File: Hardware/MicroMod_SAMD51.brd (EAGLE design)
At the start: 22 x 22 mm, 36 parts, among them J2 MICROMOD-2222, U1 W25QXX128MBIT-6X5-NO_CENTER, U2 ATSAMD51J20A-A, Y1 32.768kHz

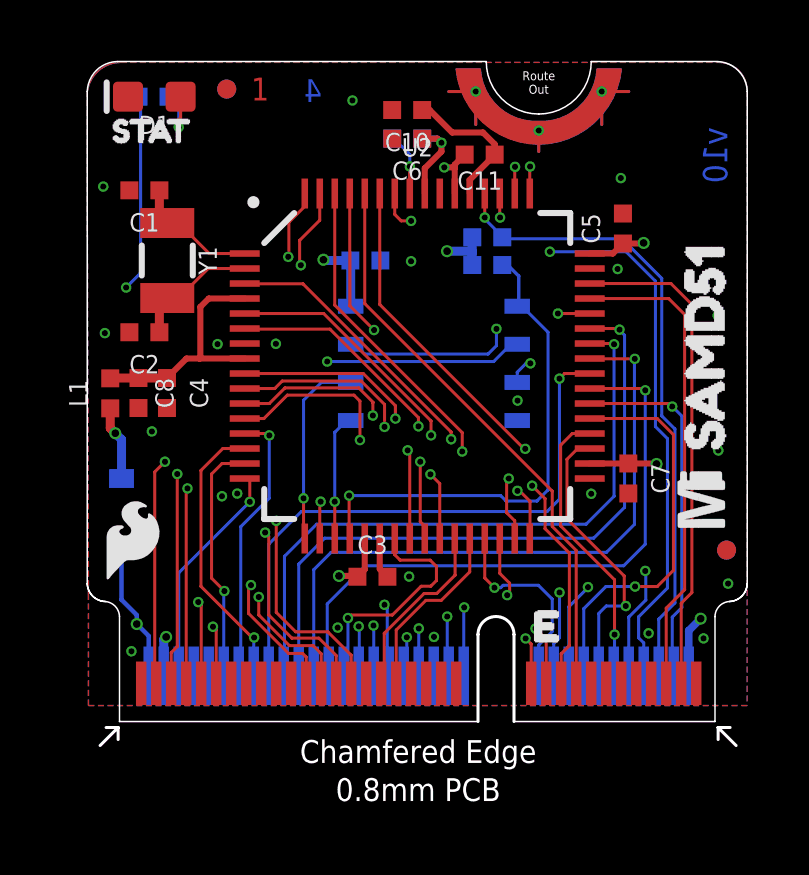
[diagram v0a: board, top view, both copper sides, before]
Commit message: Updates SparkFun silk, rolls version to v11, fixes some traces that were not crossing others at 90 degrees.
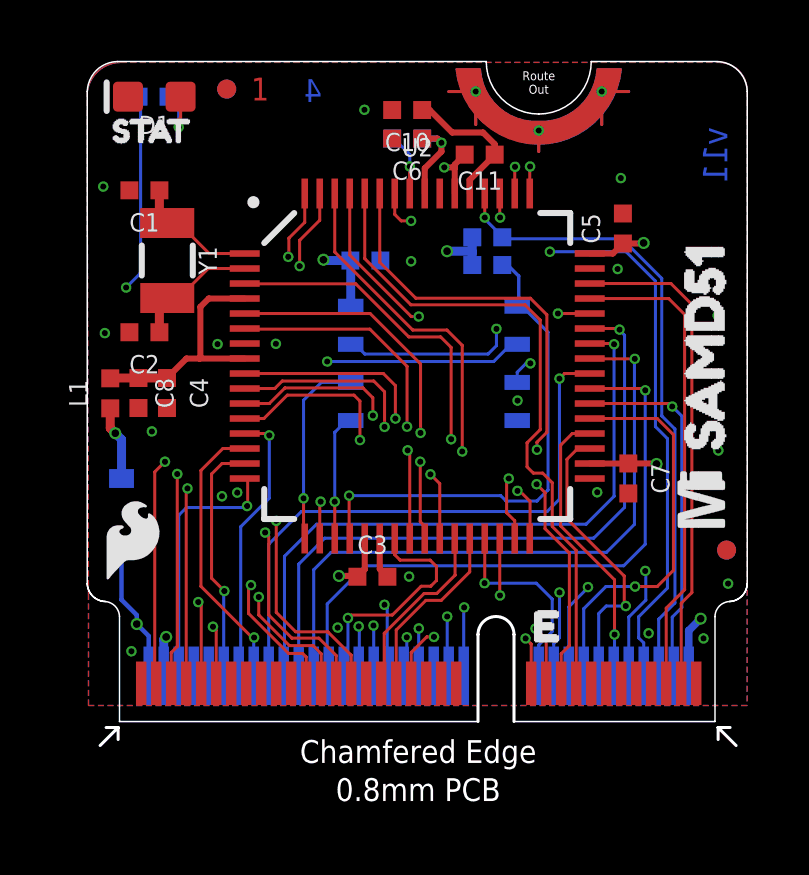
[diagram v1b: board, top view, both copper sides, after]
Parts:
- LOGO6: value SFE_LOGO_NAME_FLAME.1_INCH -> SFE_LOGO_NAME.1_INCH; device SparkFun-Aesthetics:SFE_LOGO_NAME_FLAME_.1 -> SparkFun-Aesthetics:SFE_LOGO_NAME_.1
- moved LOGO6 2.17 mm to (11.3, 7.40)
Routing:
- net TXO: track 19.2 -> 22.0 mm
- net RXI: track 19.1 -> 21.6 mm
- net GND: track 3.17 -> 5.17 mm
- net A0: track 17.1 -> 18.8 mm
- net !CS: track 7.72 -> 8.78 mm
- net D0: track 21.4 -> 22.3 mm
- net D1: track 20.2 -> 21.0 mm
- net A2/PWM0: track 17.9 -> 18.6 mm
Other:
- board text added: "v11"
- board text removed: "v10"

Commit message: Moves cap at top of board, adjusts USB differential pair
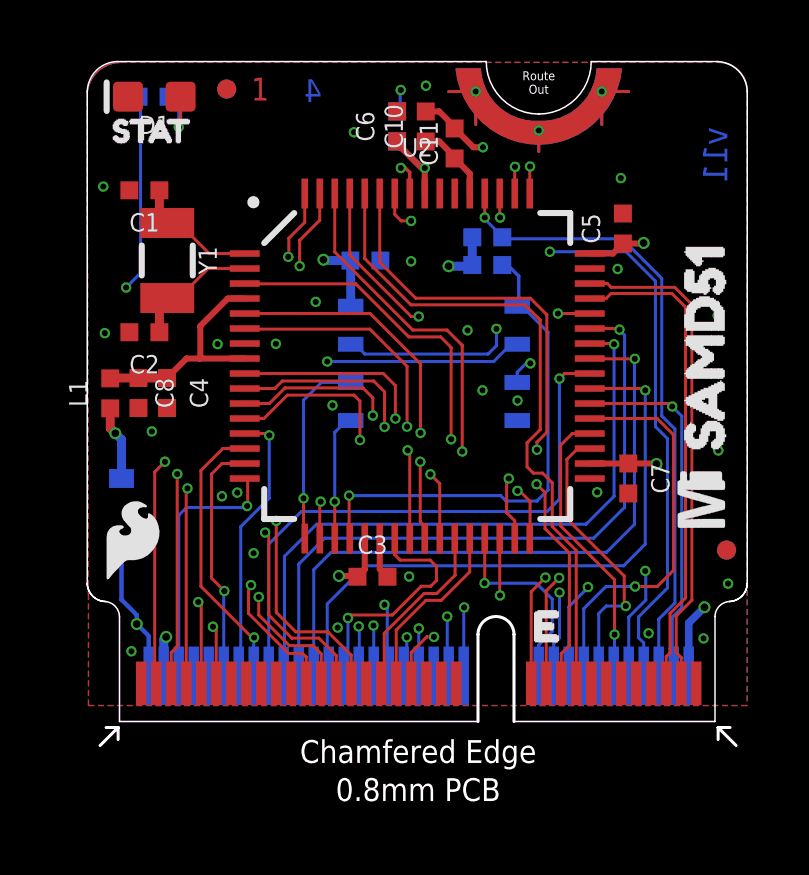
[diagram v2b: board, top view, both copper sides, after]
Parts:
- moved C11 0.91 mm to (12.2, 19.3), turned to 90 degrees
- moved C10 0.83 mm to (11.3, 19.8), turned to 90 degrees
- moved C6 0.53 mm to (10.3, 19.8), turned to 90 degrees
- moved R2 0.52 mm to (10.3, 19.8), turned to 270 degrees
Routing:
- net SWDCK: track 21.2 -> 24.8 mm, vias 2 -> 3
- net VCC: track 4.88 -> 2.61 mm
- net 3.3V_IN: track 27.9 -> 29.3 mm
- net SWDIO: track 18.4 -> 19.6 mm
- net GND: track 5.17 -> 5.76 mm, vias 21 -> 27

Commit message: Increases dimension line width, fixes some proportional text, relabels A0 to includ DAC
* Adds dimension measurements to measures layer
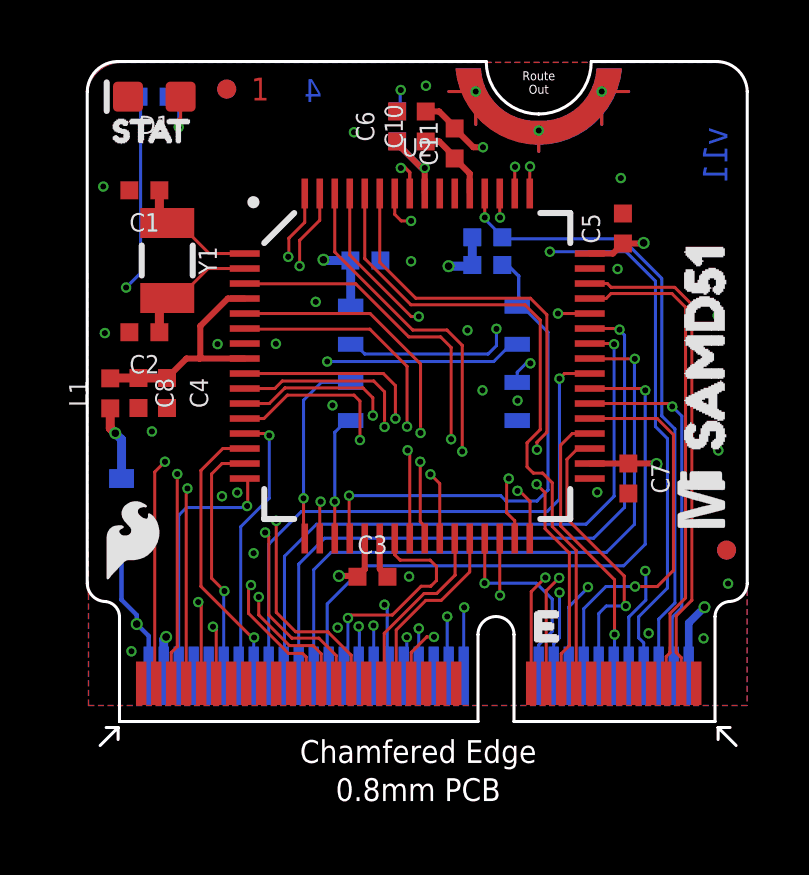
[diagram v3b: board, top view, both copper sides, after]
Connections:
- net A0 renamed A0/DAC
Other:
- board text removed: "Units in inches"
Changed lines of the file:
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@@
 <layers>
 <layer number="1" name="Top" color="4" fill="1" visible="yes" active="yes"/>
-<layer number="2" name="PWR_HORIZ" color="1" fill="3" visible="no" active="yes"/>
-<layer number="15" name="GND-VERT" color="4" fill="6" visible="no" active="yes"/>
+<layer number="2" name="PWR_HORIZ" color="1" fill="3" visible="yes" active="yes"/>
+<layer number="15" name="GND-VERT" color="4" fill="6" visible="yes" active="yes"/>
 <layer number="16" name="Bottom" color="3" fill="1" visible="yes" active="yes"/>
 <layer number="17" name="Pads" color="26" fill="1" visible="yes" active="yes"/>
@@
 <layer number="19" name="Unrouted" color="6" fill="1" visible="yes" active="yes"/>
 <layer number="20" name="Dimension" color="15" fill="1" visible="yes" active="yes"/>
-<layer number="21" name="tPlace" color="16" fill="1" visible="yes" active="yes"/>
-<layer number="22" name="bPlace" color="14" fill="1" visible="yes" active="yes"/>
+<layer number="21" name="tPlace" color="16" fill="1" visible="no" active="yes"/>
+<layer number="22" name="bPlace" color="14" fill="1" visible="no" active="yes"/>
 <layer number="23" name="tOrigins" color="15" fill="1" visible="yes" active="yes"/>
 <layer number="24" name="bOrigins" color="15" fill="1" visible="yes" active="yes"/>
@@
 <layer number="37" name="tTest" color="7" fill="1" visible="no" active="yes"/>
 <layer number="38" name="bTest" color="7" fill="1" visible="no" active="yes"/>
-<layer number="39" name="tKeepout" color="4" fill="11" visible="no" active="yes"/>
+<layer number="39" name="tKeepout" color="4" fill="11" visible="yes" active="yes"/>
 <layer number="40" name="bKeepout" color="1" fill="11" visible="no" active="yes"/>
 <layer number="41" name="tRestrict" color="4" fill="10" visible="no" active="yes"/>
@@
 <board>
 <plain>
-<text x="26.67" y="1.27" size="1.778" layer="47" font="vector" ratio="15">Units in inches</text>
-<dimension x1="0" y1="58.42" x2="0" y2="0" x3="-13.97" y3="29.21" textsize="1.27" textratio="15" layer="47" dtype="vertical" unit="inch"/>
-<dimension x1="2.54" y1="55.88" x2="0" y2="0" x3="-11.43" y3="27.94" textsize="1.27" textratio="15" layer="47" dtype="vertical" unit="inch"/>
-<dimension x1="0" y1="0" x2="2.286" y2="18.415" x3="-8.763" y3="9.2075" textsize="1.27" textratio="15" layer="47" dtype="vertical" unit="inch"/>
-<dimension x1="0" y1="0" x2="22.86" y2="0" x3="11.43" y3="-3.81" textsize="1.27" textratio="15" layer="47" dtype="horizontal" unit="inch"/>
-<dimension x1="0" y1="0" x2="2.54" y2="2.54" x3="1.27" y3="-6.35" textsize="1.27" textratio="15" layer="47" dtype="horizontal" unit="inch"/>
-<dimension x1="0" y1="0" x2="2.54" y2="2.54" x3="-6.35" y3="1.27" textsize="1.27" textratio="15" layer="47" dtype="vertical" unit="inch"/>
 <text x="31.62" y="32.94" size="1.778" layer="51" font="vector" ratio="15">0.8mm PCB
 45 degree chamfered edge
 Four layer design</text>
-<wire x1="0" y1="4.6" x2="0" y2="21" width="0.05" layer="20"/>
-<wire x1="22" y1="21" x2="22" y2="4.6" width="0.05" layer="20"/>
-<wire x1="21" y1="22" x2="22" y2="21" width="0.05" layer="20" curve="-87.205638"/>
-<wire x1="0" y1="21" x2="1" y2="22" width="0.05" layer="20" curve="-87.205638"/>
+<wire x1="0" y1="4.6" x2="0" y2="21" width="0.1016" layer="20"/>
+<wire x1="22" y1="21" x2="22" y2="4.6" width="0.1016" layer="20"/>
+<wire x1="21" y1="22" x2="22" y2="21" width="0.1016" layer="20" curve="-87.205638"/>
+<wire x1="0" y1="21" x2="1" y2="22" width="0.1016" layer="20" curve="-87.205638"/>
 <wire x1="0" y1="4.6" x2="0.6" y2="4" width="0.05" layer="20" curve="86.784874"/>
 <wire x1="21.4" y1="4" x2="22" y2="4.6" width="0.05" layer="20" curve="86.784874"/>
-<wire x1="20.925" y1="0" x2="14.225" y2="0" width="0.0508" layer="20"/>
-<wire x1="13.025" y1="0" x2="1.075" y2="0" width="0.0508" layer="20"/>
-<wire x1="1.075" y1="0" x2="1.075" y2="3.5" width="0.0508" layer="20"/>
-<wire x1="20.925" y1="3.5" x2="20.925" y2="0" width="0.0508" layer="20"/>
-<wire x1="21.4" y1="4" x2="20.925" y2="3.5" width="0.0508" layer="20" curve="84.949116"/>
-<wire x1="0.6" y1="4" x2="1.075" y2="3.5" width="0.0508" layer="20" curve="-83.820277"/>
+<wire x1="20.925" y1="0" x2="14.225" y2="0" width="0.1016" layer="20"/>
+<wire x1="13.025" y1="0" x2="1.075" y2="0" width="0.1016" layer="20"/>
+<wire x1="1.075" y1="0" x2="1.075" y2="3.5" width="0.1016" layer="20"/>
+<wire x1="20.925" y1="3.5" x2="20.925" y2="0" width="0.1016" layer="20"/>
+<wire x1="21.4" y1="4" x2="20.925" y2="3.5" width="0.1016" layer="20" curve="84.949116"/>
+<wire x1="0.6" y1="4" x2="1.075" y2="3.5" width="0.1016" layer="20" curve="-83.820277"/>
 <wire x1="14.225" y1="2.9" x2="14.225" y2="0" width="0.1016" layer="20"/>
 <wire x1="13.025" y1="2.9" x2="13.025" y2="0" width="0.1016" layer="20"/>
 <wire x1="14.225" y1="2.9" x2="13.025" y2="2.9" width="0.1016" layer="20" curve="180"/>
-<wire x1="21.4" y1="4" x2="22" y2="4.6" width="0.05" layer="20" curve="86.784874"/>
-<wire x1="0" y1="4.6" x2="0.6" y2="4" width="0.05" layer="20" curve="86.784874"/>
+<wire x1="21.4" y1="4" x2="22" y2="4.6" width="0.1016" layer="20" curve="86.784874"/>
+<wire x1="0" y1="4.6" x2="0.6" y2="4" width="0.1016" layer="20" curve="86.784874"/>
 <text x="21.336" y="19.812" size="0.8128" layer="16" font="vector" ratio="20" rot="SMR270">v11</text>
 <text x="23.114" y="-14.097" size="1.778" layer="51" font="vector">Elias Santistevan</text>
-<wire x1="1" y1="22" x2="13.3" y2="22" width="0.05" layer="20"/>
-<wire x1="16.8" y1="22" x2="21" y2="22" width="0.05" layer="20"/>
-<wire x1="13.3" y1="22" x2="15.05" y2="20.25" width="0.05" layer="20" curve="90"/>
-<wire x1="15.05" y1="20.25" x2="16.8" y2="22" width="0.05" layer="20" curve="90"/>
+<wire x1="1" y1="22" x2="13.3" y2="22" width="0.1016" layer="20"/>
+<wire x1="16.8" y1="22" x2="21" y2="22" width="0.1016" layer="20"/>
+<wire x1="13.3" y1="22" x2="15.05" y2="20.25" width="0.1016" layer="20" curve="90"/>
+<wire x1="15.05" y1="20.25" x2="16.8" y2="22" width="0.1016" layer="20" curve="90"/>
 <text x="5.461" y="20.701" size="0.762" layer="1" font="vector" ratio="15">1</text>
 <text x="6.041" y="20.681" size="0.762" layer="2" font="vector" ratio="15">2</text>
 <text x="6.651" y="20.661" size="0.762" layer="15" font="vector" ratio="15">3</text>
 <text x="7.822" y="20.651" size="0.762" layer="16" font="vector" ratio="15" rot="MR0">4</text>
+<dimension x1="13.025" y1="0" x2="1.075" y2="0" x3="7.05" y3="-5" textsize="1.27" textratio="15" layer="47" visible="yes"/>
+<dimension x1="20.925" y1="0" x2="14.225" y2="0" x3="17.575" y3="-5" textsize="1.27" textratio="15" layer="47" visible="yes"/>
+<dimension x1="20.925" y1="0" x2="21" y2="22" x3="27" y3="11" textsize="1.27" textratio="15" layer="47" dtype="vertical" visible="yes"/>
+<dimension x1="22" y1="21" x2="0" y2="21" x3="11" y3="26.5" textsize="1.27" textratio="15" layer="47" dtype="vertical" visible="yes"/>
 </plain>
 <attributes>
@@
 <wire x1="15.7806" y1="9.2126" x2="16.168" y2="9.6" width="0.1016" layer="1"/>
 </signal>
-<signal name="A0">
+<signal name="A0/DAC">
 <contactref element="J2" pad="34"/>
 <contactref element="U2" pad="3"/>

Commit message: Updates the micromodd connector and swaps the SPI pins
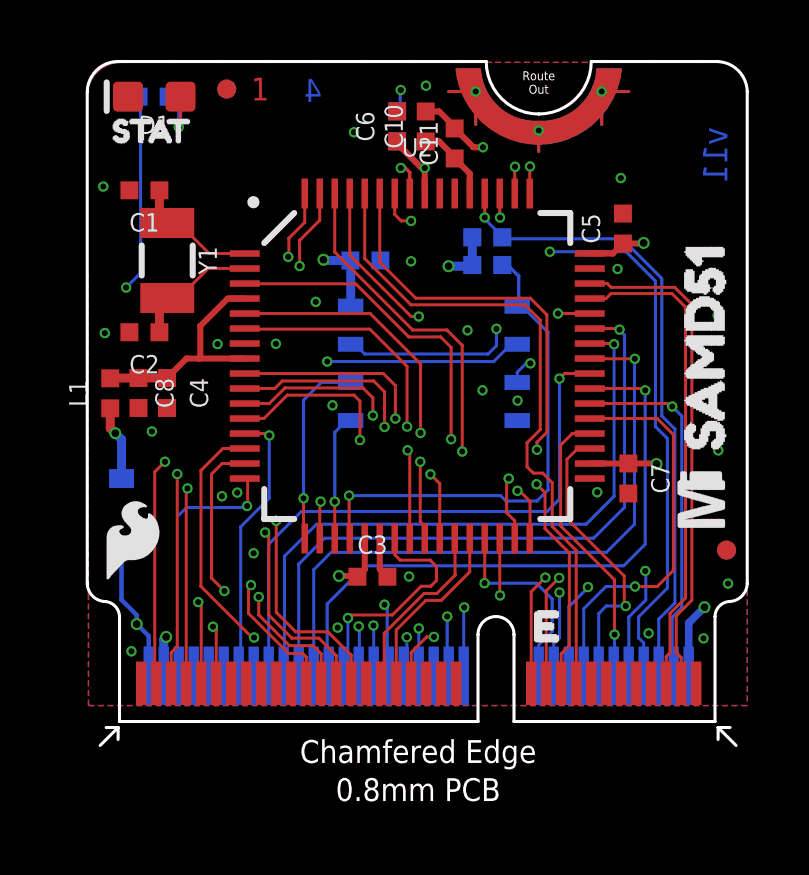
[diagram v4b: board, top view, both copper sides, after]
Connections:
- net !CS: now also J2.55; no longer J2.70
- net CIPO: now also J2.61; no longer J2.64
- net COPI: now also J2.59; no longer J2.62
- net SCLK: now also J2.57; no longer J2.60
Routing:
- net !CS: track 8.78 -> 3.43 mm
- net CIPO: track 8.16 -> 5.36 mm
- net SCLK: track 9.39 -> 8.12 mm
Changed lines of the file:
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@@
 <setting verticaltext="up"/>
 </settings>
-<grid distance="0.5" unitdist="mm" unit="mm" style="dots" multiple="1" display="yes" altdistance="0.01" altunitdist="mm" altunit="mm"/>
+<grid distance="0.05" unitdist="inch" unit="inch" style="dots" multiple="1" display="yes" altdistance="0.005" altunitdist="inch" altunit="inch"/>
 <layers>
 <layer number="1" name="Top" color="4" fill="1" visible="yes" active="yes"/>
-<layer number="2" name="PWR_HORIZ" color="1" fill="3" visible="yes" active="yes"/>
-<layer number="15" name="GND-VERT" color="4" fill="6" visible="yes" active="yes"/>
+<layer number="2" name="PWR_HORIZ" color="1" fill="3" visible="no" active="yes"/>
+<layer number="15" name="GND-VERT" color="4" fill="6" visible="no" active="yes"/>
 <layer number="16" name="Bottom" color="3" fill="1" visible="yes" active="yes"/>
 <layer number="17" name="Pads" color="26" fill="1" visible="yes" active="yes"/>
@@
 <layer number="19" name="Unrouted" color="6" fill="1" visible="yes" active="yes"/>
 <layer number="20" name="Dimension" color="15" fill="1" visible="yes" active="yes"/>
-<layer number="21" name="tPlace" color="16" fill="1" visible="no" active="yes"/>
-<layer number="22" name="bPlace" color="14" fill="1" visible="no" active="yes"/>
+<layer number="21" name="tPlace" color="16" fill="1" visible="yes" active="yes"/>
+<layer number="22" name="bPlace" color="14" fill="1" visible="yes" active="yes"/>
 <layer number="23" name="tOrigins" color="15" fill="1" visible="yes" active="yes"/>
 <layer number="24" name="bOrigins" color="15" fill="1" visible="yes" active="yes"/>
@@
 <layer number="37" name="tTest" color="7" fill="1" visible="no" active="yes"/>
 <layer number="38" name="bTest" color="7" fill="1" visible="no" active="yes"/>
-<layer number="39" name="tKeepout" color="4" fill="11" visible="yes" active="yes"/>
+<layer number="39" name="tKeepout" color="4" fill="11" visible="no" active="yes"/>
 <layer number="40" name="bKeepout" color="1" fill="11" visible="no" active="yes"/>
 <layer number="41" name="tRestrict" color="4" fill="10" visible="no" active="yes"/>
@@
 </signal>
 <signal name="COPI">
-<contactref element="J2" pad="62"/>
 <via x="6.068" y="9.5372" extent="1-16" drill="0.2"/>
 <wire x1="5.116" y1="6.4932" x2="5.116" y2="1.592" width="0.1016" layer="16"/>
-<wire x1="5.116" y1="1.592" x2="5.049" y2="1.525" width="0.1016" layer="16"/>
 <wire x1="6.068" y1="9.5372" x2="6.068" y2="7.4452" width="0.1016" layer="16"/>
 <wire x1="6.068" y1="7.4452" x2="5.116" y2="6.4932" width="0.1016" layer="16"/>
@@
 <wire x1="5.25" y1="9.6" x2="6.0052" y2="9.6" width="0.1016" layer="1"/>
 <wire x1="6.0052" y1="9.6" x2="6.068" y2="9.5372" width="0.1016" layer="1"/>
+<contactref element="J2" pad="59"/>
+<wire x1="5.799" y1="1.275" x2="5.116" y2="1.592" width="0" layer="19" extent="1-16"/>
 </signal>
 <signal name="CIPO">
-<contactref element="J2" pad="64"/>
 <wire x1="4.5714" y1="4.3496" x2="4.549" y2="4.3272" width="0.1016" layer="16"/>
-<wire x1="4.549" y1="4.3272" x2="4.549" y2="1.525" width="0.1016" layer="16"/>
 <wire x1="4.1442" y1="8.2512" x2="4.493" y2="8.6" width="0.1016" layer="1"/>
 <via x="4.5714" y="4.3496" extent="1-16" drill="0.2"/>
@@
 <contactref element="U2" pad="15"/>
 <wire x1="4.493" y1="8.6" x2="5.25" y2="8.6" width="0.1016" layer="1"/>
+<contactref element="J2" pad="61"/>
+<wire x1="5.299" y1="1.275" x2="4.549" y2="4.3272" width="0" layer="19" extent="1-16"/>
 </signal>
 <signal name="D0">
@@
 </signal>
 <signal name="SCLK" class="1">
-<contactref element="J2" pad="60"/>
 <via x="5.562" y="2.8014" extent="1-16" drill="0.2"/>
 <wire x1="5.562" y1="2.8014" x2="5.549" y2="2.7884" width="0.1016" layer="16"/>
-<wire x1="5.549" y1="2.7884" x2="5.549" y2="1.525" width="0.1016" layer="16"/>
 <wire x1="5.562" y1="2.8014" x2="5.492" y2="2.8014" width="0.1016" layer="1"/>
 <contactref element="U2" pad="14"/>
@@
 <wire x1="5.492" y1="2.8014" x2="3.79" y2="4.5034" width="0.1016" layer="1"/>
 <wire x1="3.79" y1="8.37" x2="4.52" y2="9.1" width="0.1016" layer="1"/>
+<contactref element="J2" pad="57"/>
+<wire x1="6.299" y1="1.275" x2="5.549" y2="2.7884" width="0" layer="19" extent="1-16"/>
 </signal>
 <signal name="!CS">
-<contactref element="J2" pad="70"/>
 <via x="5.3278" y="7.1834" extent="1-16" drill="0.2"/>
 <contactref element="U2" pad="16"/>
@@
 <wire x1="5.2778" y1="7.1334" x2="5.3278" y2="7.1834" width="0.1016" layer="16"/>
 <wire x1="3.3078" y1="7.1334" x2="3.049" y2="6.8746" width="0.1016" layer="16"/>
-<wire x1="3.049" y1="1.525" x2="3.049" y2="6.8746" width="0.1016" layer="16"/>
+<contactref element="J2" pad="55"/>
+<wire x1="6.799" y1="1.275" x2="5.3278" y2="7.1834" width="0" layer="19" extent="1-1"/>
 </signal>
 <signal name="I2S_FS">

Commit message: Fixes LED assignment in variant,  routes SPI lines, rolls version to v12
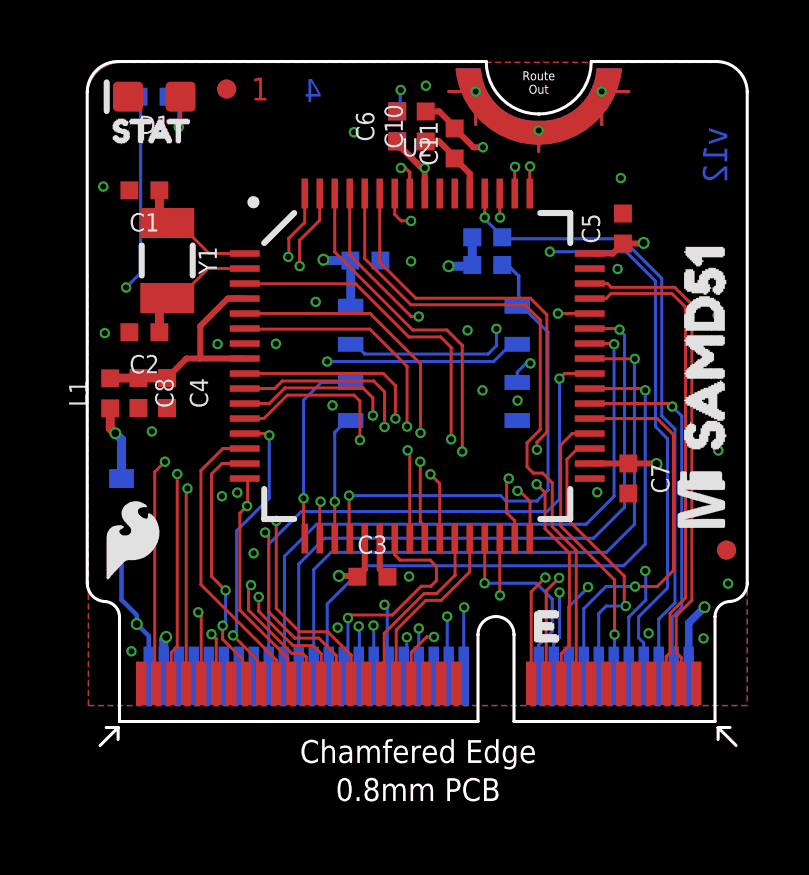
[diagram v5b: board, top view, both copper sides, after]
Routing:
- net !CS: track 3.43 -> 7.74 mm
- net CIPO: track 5.36 -> 8.79 mm, vias 1 -> 2
- net SCLK: track 8.12 -> 9.90 mm, vias 1 -> 0
- net COPI: track 9.18 -> 10.00 mm, vias 1 -> 2
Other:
- board text added: "v12"
- board text removed: "v11"
